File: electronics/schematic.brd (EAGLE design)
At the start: 20.3 x 16.5 mm, 14 parts, among them Q1 MC-405, Q3 SST201

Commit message: Small adjustments
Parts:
- moved LED+ 0.63 mm to (25.4, 17.1)
- moved LED- 0.63 mm to (25.4, 19.1)
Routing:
- net RXD: track 16.7 -> 9.79 mm
- net TXD: track 11.6 -> 8.78 mm, vias 2 -> 0
- net VCC: track 26.9 -> 28.4 mm
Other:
- board size 20.3 x 16.5 mm -> 20.3 x 16.2 mm
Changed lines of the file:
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@@
 <plain>
 <wire x1="6.35" y1="9.2075" x2="26.67" y2="9.2075" width="0.254" layer="20"/>
-<wire x1="26.67" y1="9.2075" x2="26.67" y2="25.7175" width="0.254" layer="20"/>
-<wire x1="26.67" y1="25.7175" x2="6.35" y2="25.7175" width="0.254" layer="20"/>
-<wire x1="6.35" y1="9.2075" x2="6.35" y2="25.7175" width="0.254" layer="20"/>
+<wire x1="26.67" y1="9.2075" x2="26.67" y2="25.4" width="0.254" layer="20"/>
+<wire x1="26.67" y1="25.4" x2="6.35" y2="25.4" width="0.254" layer="20"/>
+<wire x1="6.35" y1="9.2075" x2="6.35" y2="25.4" width="0.254" layer="20"/>
 <dimension x1="6.35" y1="8.89" x2="26.67" y2="8.89" x3="16.51" y3="5.08" textsize="1.778" layer="1"/>
 <dimension x1="26.67" y1="8.89" x2="26.67" y2="25.4" x3="34.925" y3="17.145" textsize="1.778" layer="1"/>
@@
 <attribute name="VALUE" x="6.858" y="9.779" size="0.0254" layer="27"/>
 </element>
-<element name="LED+" library="testpad" package="TP15R" value="TPTP15R" x="24.765" y="17.145">
-<attribute name="TP_SIGNAL_NAME" value="" x="24.765" y="17.145" size="1.778" layer="27" display="off"/>
-</element>
-<element name="LED-" library="testpad" package="TP15R" value="TPTP15R" x="24.765" y="19.05">
-<attribute name="TP_SIGNAL_NAME" value="" x="24.765" y="19.05" size="1.778" layer="27" display="off"/>
+<element name="LED+" library="testpad" package="TP15R" value="TPTP15R" x="25.4" y="17.145">
+<attribute name="TP_SIGNAL_NAME" value="" x="25.4" y="17.145" size="1.778" layer="27" display="off"/>
+</element>
+<element name="LED-" library="testpad" package="TP15R" value="TPTP15R" x="25.4" y="19.05">
+<attribute name="TP_SIGNAL_NAME" value="" x="25.4" y="19.05" size="1.778" layer="27" display="off"/>
 </element>
 <element name="VCC2" library="testpad" package="TP15R" value="TPTP15R" x="25.4" y="14.605">
@@
 <wire x1="24.003" y1="13.5255" x2="24.765" y2="14.2875" width="0.254" layer="1"/>
 <wire x1="24.765" y1="14.2875" x2="25.4" y2="14.605" width="0.254" layer="1"/>
-<wire x1="24.765" y1="15.875" x2="24.765" y2="17.145" width="0" layer="19" extent="1-1"/>
 <wire x1="22.86" y1="12.38" x2="23.561" y2="13.081" width="0.254" layer="1"/>
+<wire x1="24.765" y1="15.875" x2="24.765" y2="16.51" width="0.254" layer="1"/>
+<wire x1="24.765" y1="16.51" x2="25.4" y2="17.145" width="0.254" layer="1"/>
 </signal>
 <signal name="TXD">
 <contactref element="U$1" pad="15"/>
 <contactref element="TXD" pad="TP"/>
-<wire x1="7.62" y1="20.955" x2="9.271" y2="19.304" width="0.254" layer="1"/>
-<wire x1="9.271" y1="19.304" x2="11.43" y2="19.304" width="0.254" layer="1"/>
-<via x="11.43" y="19.304" extent="1-16" drill="0.6" shape="square"/>
-<wire x1="11.43" y1="19.304" x2="15.875" y2="19.304" width="0.254" layer="16"/>
-<via x="15.875" y="19.304" extent="1-16" drill="0.6" shape="square"/>
-<wire x1="15.875" y1="19.304" x2="15.875" y2="21.995" width="0.254" layer="1"/>
+<wire x1="7.62" y1="20.955" x2="8.255" y2="20.955" width="0.254" layer="1"/>
+<wire x1="8.255" y1="20.955" x2="8.89" y2="20.32" width="0.254" layer="1"/>
+<wire x1="8.89" y1="20.32" x2="15.24" y2="20.32" width="0.254" layer="1"/>
+<wire x1="15.24" y1="20.32" x2="15.875" y2="20.955" width="0.254" layer="1"/>
+<wire x1="15.875" y1="20.955" x2="15.875" y2="21.995" width="0" layer="19" extent="1-16"/>
 </signal>
 <signal name="RXD">
 <contactref element="U$1" pad="14"/>
 <contactref element="RXD" pad="TP"/>
-<wire x1="7.62" y1="23.495" x2="8.89" y2="22.225" width="0.254" layer="1"/>
-<wire x1="8.89" y1="22.225" x2="8.89" y2="20.955" width="0.254" layer="1"/>
-<wire x1="8.89" y1="20.955" x2="9.525" y2="20.32" width="0.254" layer="1"/>
-<wire x1="9.525" y1="20.32" x2="13.335" y2="20.32" width="0.254" layer="1"/>
-<wire x1="13.335" y1="20.32" x2="13.97" y2="19.685" width="0.254" layer="1"/>
-<wire x1="13.97" y1="19.685" x2="13.97" y2="18.415" width="0.254" layer="1"/>
-<wire x1="13.97" y1="18.415" x2="17.145" y2="18.415" width="0.254" layer="1"/>
-<wire x1="17.145" y1="18.415" x2="17.145" y2="21.995" width="0.254" layer="1"/>
+<wire x1="7.62" y1="23.495" x2="16.51" y2="23.495" width="0.254" layer="1"/>
+<wire x1="16.51" y1="23.495" x2="17.145" y2="22.86" width="0.254" layer="1"/>
+<wire x1="17.145" y1="22.86" x2="17.145" y2="21.995" width="0" layer="19" extent="1-16"/>
 </signal>
 <signal name="LED">
@@
 <wire x1="22.8625" y1="21.76" x2="23.1345" y2="21.76" width="0.254" layer="1"/>
 <wire x1="23.1345" y1="21.76" x2="24.765" y2="20.1295" width="0.254" layer="1"/>
-<wire x1="24.765" y1="20.1295" x2="24.765" y2="19.05" width="0.254" layer="1"/>
+<wire x1="24.765" y1="20.1295" x2="25.4" y2="19.05" width="0.254" layer="1"/>
 </signal>
 </signals>

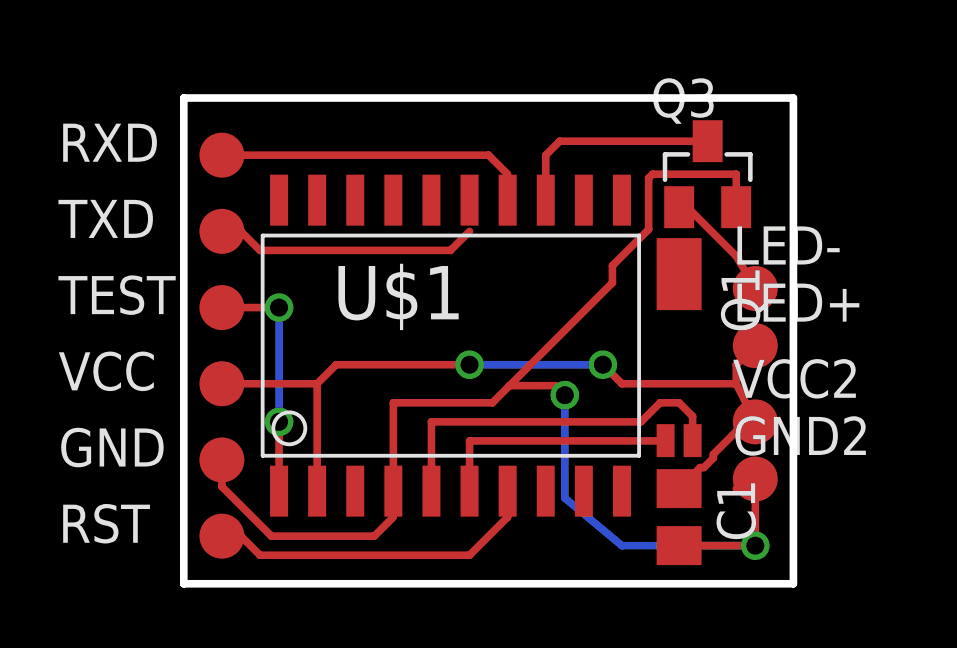
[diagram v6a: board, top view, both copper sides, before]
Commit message: Rotated FET
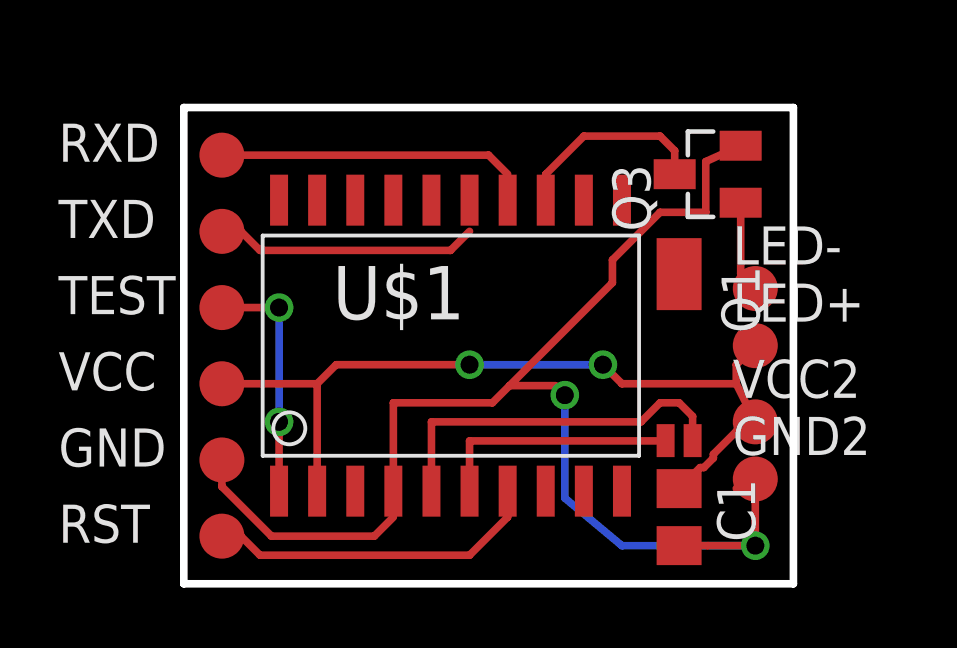
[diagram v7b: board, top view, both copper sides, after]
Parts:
- turned Q3 to 90 degrees
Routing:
- net N$4: track 3.83 -> 3.06 mm
- net GND: track 45.3 -> 44.8 mm
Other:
- board size 20.3 x 16.2 mm -> 20.3 x 15.9 mm
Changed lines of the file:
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@@
 <plain>
 <wire x1="6.35" y1="9.2075" x2="26.67" y2="9.2075" width="0.254" layer="20"/>
-<wire x1="26.67" y1="9.2075" x2="26.67" y2="25.4" width="0.254" layer="20"/>
-<wire x1="26.67" y1="25.4" x2="6.35" y2="25.4" width="0.254" layer="20"/>
-<wire x1="6.35" y1="9.2075" x2="6.35" y2="25.4" width="0.254" layer="20"/>
+<wire x1="26.67" y1="9.2075" x2="26.67" y2="25.0825" width="0.254" layer="20"/>
+<wire x1="26.67" y1="25.0825" x2="6.35" y2="25.0825" width="0.254" layer="20"/>
+<wire x1="6.35" y1="9.2075" x2="6.35" y2="25.0825" width="0.254" layer="20"/>
 <dimension x1="6.35" y1="8.89" x2="26.67" y2="8.89" x3="16.51" y3="5.08" textsize="1.778" layer="1"/>
 <dimension x1="26.67" y1="8.89" x2="26.67" y2="25.4" x3="34.925" y3="17.145" textsize="1.778" layer="1"/>
@@
 </element>
 <element name="U$1" library="TI_MSP430_v16" package="DW20" value="F21X1---DW20" x="15.24" y="17.145"/>
-<element name="Q3" library="transistor-fet" package="SOT23" value="SST201" x="23.8125" y="22.86"/>
+<element name="Q3" library="transistor-fet" package="SOT23" value="SST201" x="23.8125" y="22.86" rot="R90"/>
 <element name="RXD" library="testpad" package="TP15R" value="TPTP15R" x="7.62" y="23.495" smashed="yes">
 <attribute name="TP_SIGNAL_NAME" value="" x="7.62" y="20.955" size="1" layer="37"/>
@@
 <contactref element="U$1" pad="13"/>
 <contactref element="Q3" pad="3"/>
-<wire x1="18.415" y1="21.995" x2="18.415" y2="23.495" width="0.254" layer="1"/>
-<wire x1="18.415" y1="23.495" x2="18.88" y2="23.96" width="0.254" layer="1"/>
-<wire x1="18.88" y1="23.96" x2="23.8125" y2="23.96" width="0.254" layer="1"/>
+<wire x1="22.7125" y1="22.86" x2="22.7125" y2="23.6425" width="0.254" layer="1"/>
+<wire x1="22.7125" y1="23.6425" x2="22.225" y2="24.13" width="0.254" layer="1"/>
+<wire x1="22.225" y1="24.13" x2="19.685" y2="24.13" width="0.254" layer="1"/>
+<wire x1="19.685" y1="24.13" x2="18.415" y2="22.86" width="0.254" layer="1"/>
+<wire x1="18.415" y1="22.86" x2="18.415" y2="21.995" width="0.254" layer="1"/>
 </signal>
 <signal name="GND">
@@
 <contactref element="C1" pad="2"/>
 <wire x1="24.765" y1="12.385" x2="25.4" y2="12.7" width="0.254" layer="1"/>
-<wire x1="24.7625" y1="21.76" x2="24.765" y2="21.7625" width="0.254" layer="1"/>
-<wire x1="24.765" y1="21.7625" x2="24.765" y2="22.86" width="0.254" layer="1"/>
-<wire x1="24.765" y1="22.86" x2="21.971" y2="22.86" width="0.254" layer="1"/>
-<wire x1="21.971" y1="22.86" x2="21.844" y2="22.733" width="0.254" layer="1"/>
-<wire x1="21.844" y1="22.733" x2="21.844" y2="21.0185" width="0.254" layer="1"/>
-<wire x1="21.844" y1="21.0185" x2="20.6375" y2="19.812" width="0.254" layer="1"/>
-<wire x1="20.6375" y1="19.812" x2="20.6375" y2="19.2405" width="0.254" layer="1"/>
 <wire x1="22.86" y1="10.48" x2="23.815" y2="10.48" width="0.254" layer="1"/>
 <wire x1="23.815" y1="10.48" x2="25.4" y2="10.4775" width="0.254" layer="1"/>
 <wire x1="13.335" y1="11.43" x2="13.335" y2="12.295" width="0" layer="19" extent="1-1"/>
+<wire x1="20.6375" y1="19.2405" x2="20.6375" y2="20.0025" width="0.254" layer="1"/>
+<wire x1="20.6375" y1="20.0025" x2="22.225" y2="21.59" width="0.254" layer="1"/>
+<wire x1="22.225" y1="21.59" x2="23.749" y2="21.59" width="0.254" layer="1"/>
+<wire x1="23.749" y1="21.59" x2="23.749" y2="23.2815" width="0.254" layer="1"/>
+<wire x1="23.749" y1="23.2815" x2="24.9125" y2="23.81" width="0.254" layer="1"/>
 </signal>
 <signal name="N$4">
 <contactref element="Q3" pad="1"/>
 <contactref element="LED-" pad="TP"/>
-<wire x1="22.8625" y1="21.76" x2="23.1345" y2="21.76" width="0.254" layer="1"/>
-<wire x1="23.1345" y1="21.76" x2="24.765" y2="20.1295" width="0.254" layer="1"/>
-<wire x1="24.765" y1="20.1295" x2="25.4" y2="19.05" width="0.254" layer="1"/>
+<wire x1="24.9125" y1="21.91" x2="24.9125" y2="19.5375" width="0.254" layer="1"/>
+<wire x1="24.9125" y1="19.5375" x2="25.4" y2="19.05" width="0.254" layer="1"/>
 </signal>
 </signals>

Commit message: RC0. Actual MOSTFET. Added sync pulse. Included LEDs
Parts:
- removed LED+, LED-: TPTP15R, testpad:TP15R
- removed Q1: MC-405, ROB:MC-405
- removed Q3: SST201, transistor-fet:SOT23
- added LED1, LED2, LED3, LED4: (no value), led:CHIP-LED0805
- added Q2: NX3008NBK, playafly:SOT23
- added R1, R2, R3, R4: (no value), resistor:M0805
- added SYNC0, SYNC1: TPTP15R, testpad:TP15R
- added U$2: AB26TRQ, playafly:QUARZ5
- renumbered GND2 to VBAT-, VCC2 to VBAT+
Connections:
- removed net N$1: Q1.P$3, U$1.5
- removed net N$2: Q1.P$6, U$1.6
- new net N$5: LED2.C, R2.2
- new net N$6: LED3.C, R3.2
- new net N$7: LED4.C, R4.2
- new net N$8: Q2.3, R1.1, R2.1, R3.1, R4.1
- new net P2.0: SYNC0.TP, U$1.8
- new net XIN: U$1.6, U$2.P$1
- new net XOUT: U$1.5, U$2.P$2
- net GND: now also Q2.2, SYNC1.TP, U$2.GND@3; no longer Q3.2
- net LED: now also Q2.1; no longer Q3.3
- net N$4: now also LED1.C, R1.2; no longer LED-.TP, Q3.1
- net RST: no longer U$1.7
- net VCC: now also LED1.A, LED2.A, LED3.A, LED4.A, U$1.7; no longer LED+.TP
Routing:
- net N$1: track 12.4 -> 0.00 mm
- net XOUT: track 0.00 -> 11.5 mm
- net N$2: track 8.48 -> 0.00 mm
- net XIN: track 0.00 -> 8.29 mm
- net N$4: track 3.06 -> 0.00 mm
- net TXD: track 8.78 -> 10.2 mm
- net VCC: track 28.4 -> 27.5 mm
- net RST: track 11.2 -> 10.3 mm
- net RXD: track 9.79 -> 10.7 mm
- net LED: track 6.67 -> 5.89 mm
